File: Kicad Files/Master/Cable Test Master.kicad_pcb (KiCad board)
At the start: 2 copper layers, 50.8 x 62.2 mm, 64 parts, among them J1 RJ45, J2 RJ12, J3 PWR, J4 ISP, Q1 BSS84, Q10 2N7002, Q11 2N7002, Q12 2N7002, Q13 2N7002, Q14 2N7002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

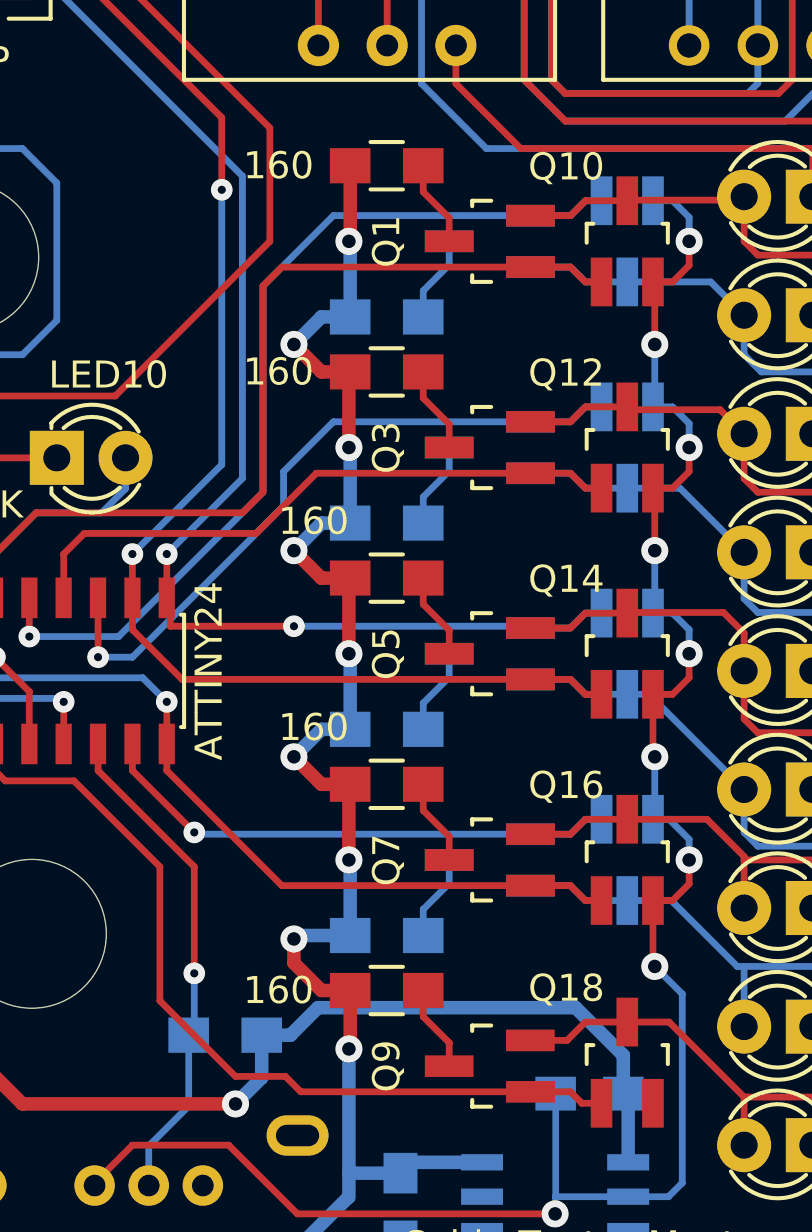
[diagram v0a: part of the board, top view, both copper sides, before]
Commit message: Fix P-channel MOSFET wiring and software output levels
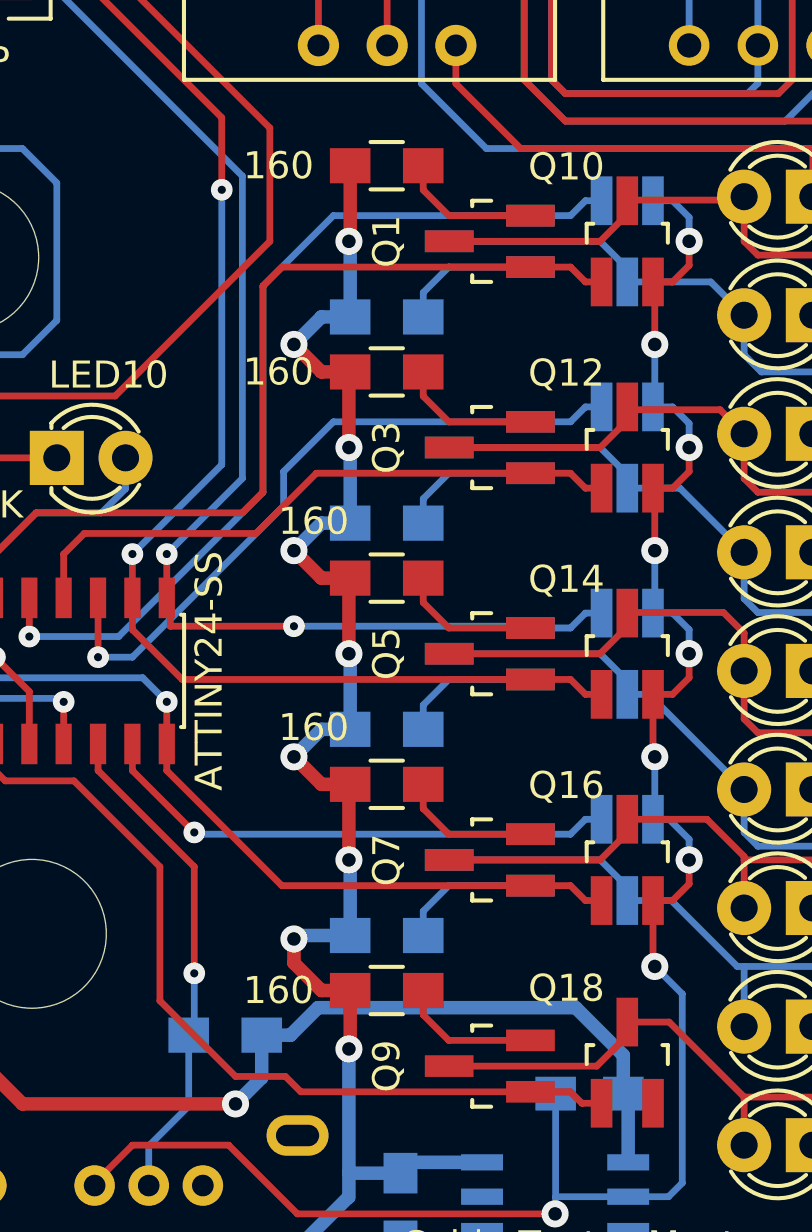
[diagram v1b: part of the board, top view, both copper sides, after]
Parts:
- U1: value ATTINY24 -> ATTINY24-SS
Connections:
- Q1 pad 2: /MOSFET Drive/DRIVE_1 -> Net-(Q1-Pad2)
- Q1 pad 3: Net-(Q1-Pad3) -> /MOSFET Drive/DRIVE_1
- Q2 pad 2: /MOSFET Drive/DRIVE_2 -> Net-(Q2-Pad2)
- Q2 pad 3: Net-(Q2-Pad3) -> /MOSFET Drive/DRIVE_2
- Q3 pad 2: /MOSFET Drive/DRIVE_3 -> Net-(Q3-Pad2)
- Q3 pad 3: Net-(Q3-Pad3) -> /MOSFET Drive/DRIVE_3
- Q4 pad 2: /MOSFET Drive/DRIVE_4 -> Net-(Q4-Pad2)
- Q4 pad 3: Net-(Q4-Pad3) -> /MOSFET Drive/DRIVE_4
- Q5 pad 2: /MOSFET Drive/DRIVE_5 -> Net-(Q5-Pad2)
- Q5 pad 3: Net-(Q5-Pad3) -> /MOSFET Drive/DRIVE_5
- Q6 pad 2: /MOSFET Drive/DRIVE_6 -> Net-(Q6-Pad2)
- Q6 pad 3: Net-(Q6-Pad3) -> /MOSFET Drive/DRIVE_6
- Q7 pad 2: /MOSFET Drive/DRIVE_7 -> Net-(Q7-Pad2)
- Q7 pad 3: Net-(Q7-Pad3) -> /MOSFET Drive/DRIVE_7
- Q8 pad 2: /MOSFET Drive/DRIVE_8 -> Net-(Q8-Pad2)
- Q8 pad 3: Net-(Q8-Pad3) -> /MOSFET Drive/DRIVE_8
- Q9 pad 2: /MOSFET Drive/DRIVE_S -> Net-(Q9-Pad2)
- Q9 pad 3: Net-(Q9-Pad3) -> /MOSFET Drive/DRIVE_S
- R1 pad 2: Net-(Q1-Pad3) -> Net-(Q1-Pad2)
- R2 pad 2: Net-(Q2-Pad3) -> Net-(Q2-Pad2)
- R3 pad 2: Net-(Q3-Pad3) -> Net-(Q3-Pad2)
- R4 pad 2: Net-(Q4-Pad3) -> Net-(Q4-Pad2)
- R5 pad 2: Net-(Q5-Pad3) -> Net-(Q5-Pad2)
- R6 pad 2: Net-(Q6-Pad3) -> Net-(Q6-Pad2)
- R7 pad 2: Net-(Q7-Pad3) -> Net-(Q7-Pad2)
- R8 pad 2: Net-(Q8-Pad3) -> Net-(Q8-Pad2)
- R9 pad 2: Net-(Q9-Pad3) -> Net-(Q9-Pad2)
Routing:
- net Net-(Q9-Pad2): track 0.00 -> 5.25 mm
- net Net-(Q4-Pad2): track 0.00 -> 5.25 mm
- net Net-(Q3-Pad2): track 0.00 -> 5.25 mm
- net Net-(Q8-Pad2): track 0.00 -> 5.25 mm
- net Net-(Q5-Pad2): track 0.00 -> 5.25 mm
- net Net-(Q2-Pad2): track 0.00 -> 5.25 mm
- net Net-(Q7-Pad2): track 0.00 -> 5.25 mm
- net Net-(Q6-Pad2): track 0.00 -> 5.25 mm
- net Net-(Q1-Pad2): track 0.00 -> 5.25 mm
- net /MOSFET Drive/DRIVE_7: track 18.6 -> 22.3 mm
- net /MOSFET Drive/DRIVE_6: track 20.0 -> 23.6 mm
- net /MOSFET Drive/DRIVE_5: track 19.7 -> 23.4 mm
- net /MOSFET Drive/DRIVE_4: track 19.7 -> 23.4 mm
- net /MOSFET Drive/DRIVE_1: track 23.5 -> 27.2 mm
- net /MOSFET Drive/DRIVE_8: track 20.1 -> 23.8 mm
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
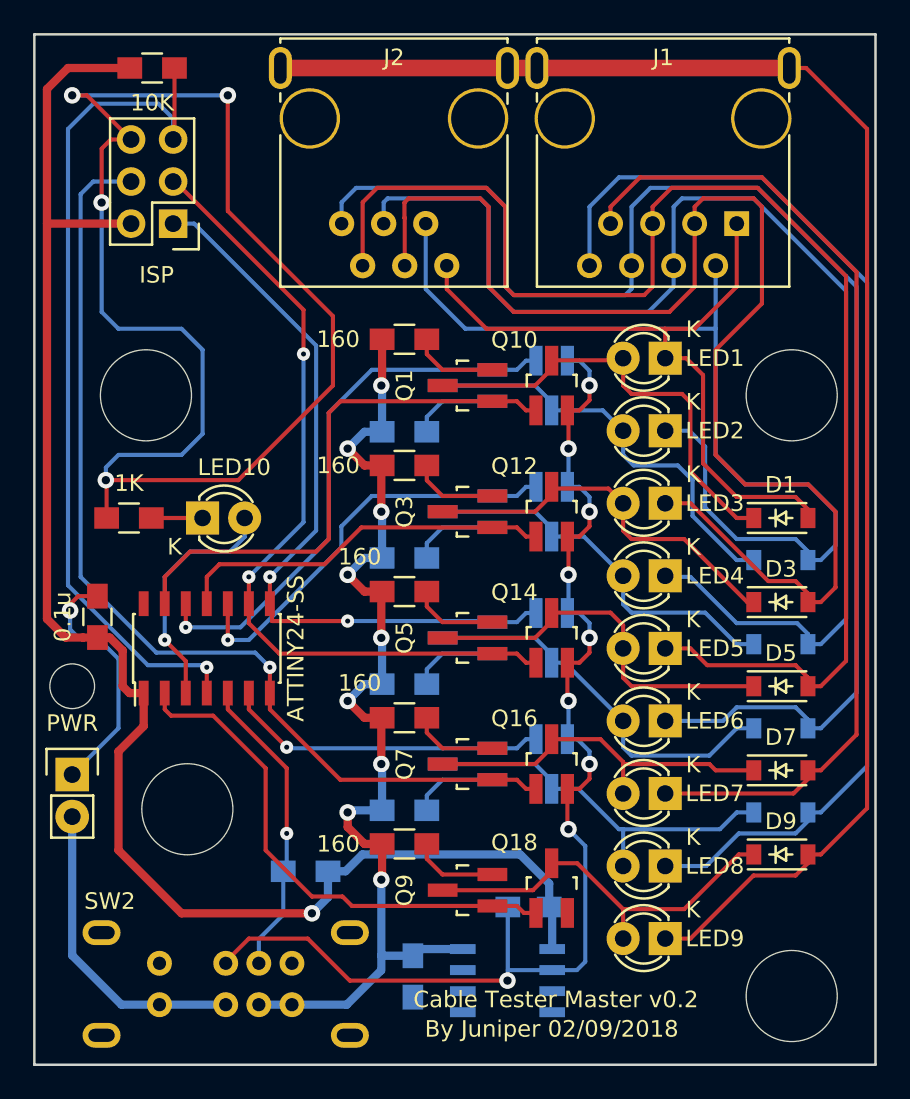
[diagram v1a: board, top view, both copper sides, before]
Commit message: Improve fit and finish issues
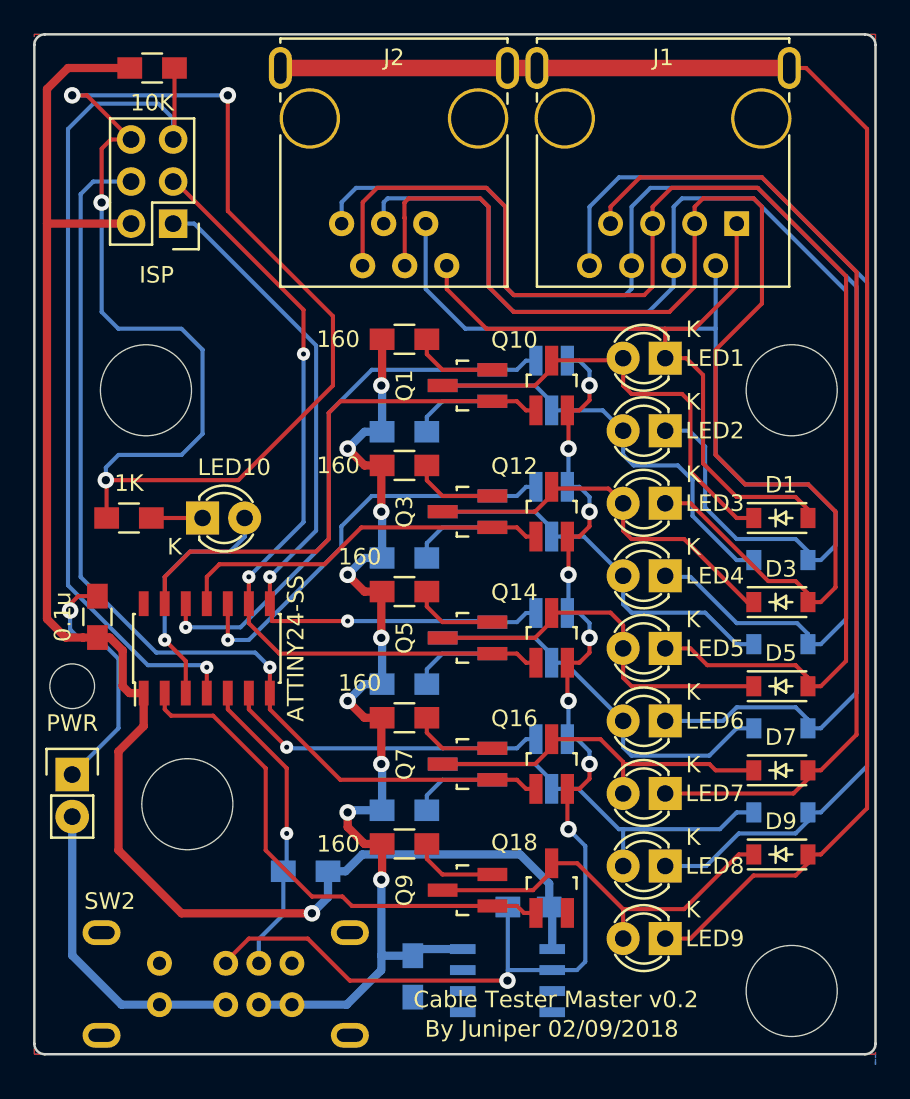
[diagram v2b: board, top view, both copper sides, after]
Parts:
- moved REF** 0.30 mm to (121.0, 110.0)
- moved REF** 0.30 mm to (157.5, 121.3)
- moved REF** 0.30 mm to (157.5, 85.0)
- moved REF** 0.30 mm to (118.5, 85.0)
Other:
- board size 50.8 x 62.2 mm -> 50.8 x 61.6 mm
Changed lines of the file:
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@@
     (links 131)
     (no_connects 0)
-    (area 111.684999 63.424999 162.635001 125.805001)
+    (area 105.560536 62.307 166.084524 129.55524)
     (thickness 1.6)
-    (drawings 6)
+    (drawings 10)
     (tracks 606)
     (zones 0)
@@
   )
   (module Mounting_Holes:MountingHole_5-5mm locked (layer F.Cu)
-    (at 121 110.3)
+    (at 121 109.9952)
     (descr "Mounting hole, Befestigungsbohrung, 5,5mm, No Annular, Kein Restring,")
     (tags "Mounting hole, Befestigungsbohrung, 5,5mm, No Annular, Kein Restring,")
@@
   )
   (module Mounting_Holes:MountingHole_5-5mm locked (layer F.Cu)
-    (at 157.5 121.58)
+    (at 157.5 121.2752)
     (descr "Mounting hole, Befestigungsbohrung, 5,5mm, No Annular, Kein Restring,")
     (tags "Mounting hole, Befestigungsbohrung, 5,5mm, No Annular, Kein Restring,")
@@
   )
   (module Mounting_Holes:MountingHole_5-5mm locked (layer F.Cu)
-    (at 157.5 85.3)
+    (at 157.5 84.9952)
     (descr "Mounting hole, Befestigungsbohrung, 5,5mm, No Annular, Kein Restring,")
     (tags "Mounting hole, Befestigungsbohrung, 5,5mm, No Annular, Kein Restring,")
@@
   )
   (module Mounting_Holes:MountingHole_5-5mm locked (layer F.Cu)
-    (at 118.5 85.3)
+    (at 118.5 84.9952)
     (descr "Mounting hole, Befestigungsbohrung, 5,5mm, No Annular, Kein Restring,")
     (tags "Mounting hole, Befestigungsbohrung, 5,5mm, No Annular, Kein Restring,")
@@
     (pad 1 thru_hole circle (at 0 0) (size 2.7 2.7) (drill 2.7) (layers))
   )
+  (gr_line (start 111.76 124.46) (end 111.76 64.135) (layer Edge.Cuts) (width 0.15))
+  (gr_line (start 162.56 64.135) (end 162.56 124.46) (layer Edge.Cuts) (width 0.15))
+  (gr_line (start 112.395 63.5) (end 161.925 63.5) (layer Edge.Cuts) (width 0.15))
+  (gr_line (start 112.395 125.095) (end 161.925 125.095) (layer Edge.Cuts) (width 0.15))
+  (gr_arc (start 112.395 124.46) (end 112.395 125.095) (angle 90) (layer Edge.Cuts) (width 0.15))
+  (gr_arc (start 161.925 124.46) (end 162.56 124.46) (angle 90) (layer Edge.Cuts) (width 0.15))
+  (gr_arc (start 161.925 64.135) (end 161.925 63.5) (angle 90) (layer Edge.Cuts) (width 0.15))
+  (gr_arc (start 112.395 64.135) (end 111.76 64.135) (angle 90) (layer Edge.Cuts) (width 0.15))
   (gr_text "By Juniper 02/09/2018" (at 143.002 123.571) (layer F.SilkS)
     (effects (font (size 1 1) (thickness 0.2)))
@@
     (effects (font (size 1 1) (thickness 0.2)))
   )
-  (gr_line (start 162.56 63.5) (end 162.56 125.73) (angle 90) (layer Edge.Cuts) (width 0.15))
-  (gr_line (start 111.76 125.73) (end 111.76 63.5) (angle 90) (layer Edge.Cuts) (width 0.15))
-  (gr_line (start 111.76 125.73) (end 162.56 125.73) (angle 90) (layer Edge.Cuts) (width 0.15))
-  (gr_line (start 162.56 63.5) (end 111.76 63.5) (angle 90) (layer Edge.Cuts) (width 0.15))
   (segment (start 132.762 110.363) (end 130.81 110.363) (width 0.5) (layer B.Cu) (net 1))
   (segment (start 130.81 110.363) (end 130.683 110.49) (width 0.5) (layer B.Cu) (net 1))
@@
     (polygon
       (pts
-        (xy 162.56 125.73) (xy 111.76 125.73) (xy 111.76 63.5) (xy 162.56 63.5) (xy 162.56 125.73)
+        (xy 162.56 125.095) (xy 111.76 125.095) (xy 111.76 63.5) (xy 162.56 63.5) (xy 162.56 125.095)
       )
     )
@@
     (polygon
       (pts
-        (xy 162.56 125.73) (xy 111.76 125.73) (xy 111.76 63.5) (xy 162.56 63.5) (xy 162.56 125.73)
+        (xy 162.56 125.095) (xy 111.76 125.095) (xy 111.76 63.5) (xy 162.56 63.5) (xy 162.56 125.73)
       )
     )

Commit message: Update Component Positioning on Master PCB
Updates the positioning of components to fix positioning issues introduced
by the earlier shortening of the board to improve fit.
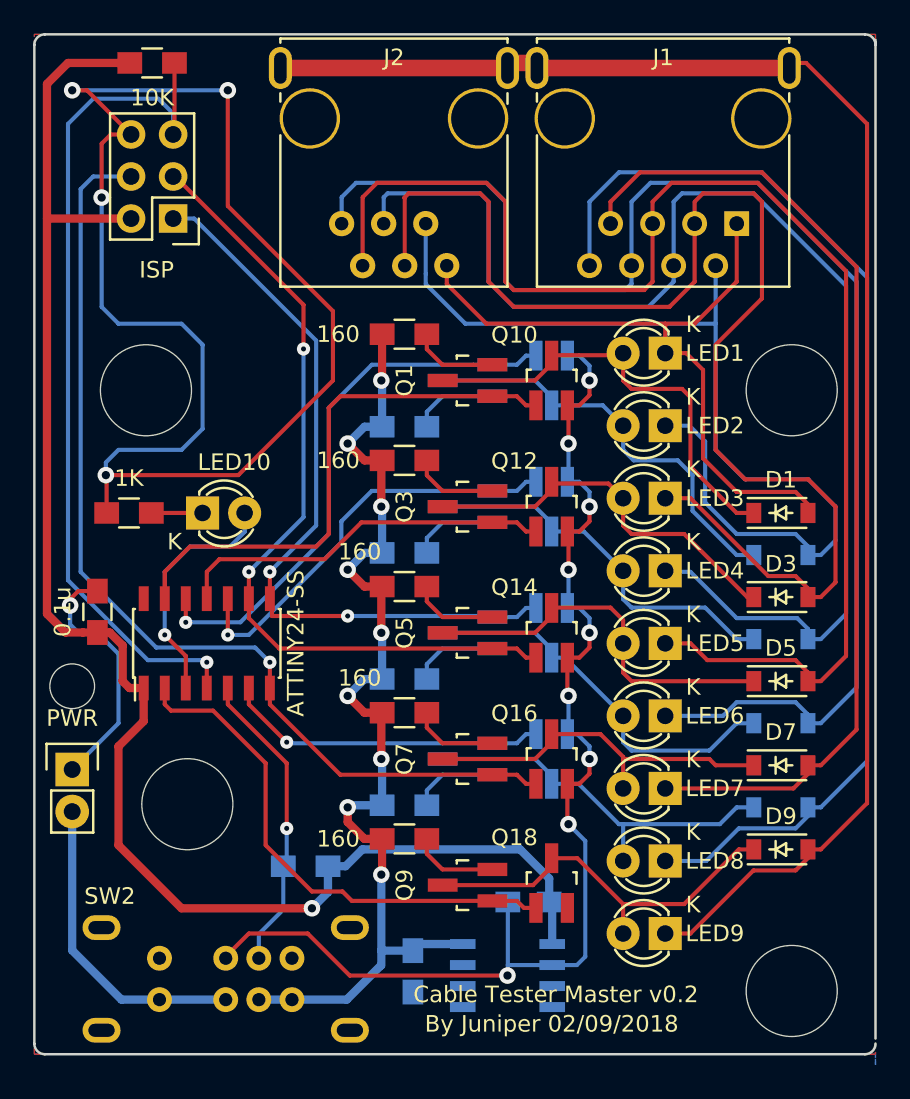
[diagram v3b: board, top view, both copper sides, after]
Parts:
- moved C1 0.30 mm to (134.6, 120.1)
- moved C2 0.30 mm to (141.6, 115.9)
- moved C3 0.30 mm to (115.6, 98.4)
- moved D1 0.30 mm to (156.8, 92.4)
- moved D2 0.30 mm to (156.8, 94.9)
- moved D3 0.30 mm to (156.8, 97.5)
- moved D4 0.30 mm to (156.8, 100.0)
- moved D5 0.30 mm to (156.8, 102.6)
- moved D6 0.30 mm to (156.8, 105.1)
- moved D7 0.30 mm to (156.8, 107.6)
- moved D8 0.30 mm to (156.8, 110.2)
- moved D9 0.30 mm to (156.8, 112.7)
- moved J3 0.30 mm to (114.0, 107.9)
- moved J4 0.30 mm to (120.1, 74.6)
- moved LED1 0.30 mm to (149.9, 82.8)
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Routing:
- net /2: track 61.5 -> 60.8 mm
- net /1: track 42.6 -> 42.0 mm
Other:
- outline, holes or cut-outs redrawn
